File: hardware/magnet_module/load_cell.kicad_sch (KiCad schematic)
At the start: 12 parts, among them J7 691137710004, U4 NAU7802, U5 KC2520Z4.91520C1KX00

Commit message: add titles & esd protection for IO
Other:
- company: (none) -> Christie Lab, CU-Anschultz
- title: (none) -> Autotrainer Magnet Module - Load Cell
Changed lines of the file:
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@@
 	(generator_version "8.0")
 	(paper "A4")
+	(title_block
+		(title "Autotrainer Magnet Module - Load Cell")
+		(date "2024-07-09")
+		(rev "v1.0")
+		(company "Christie Lab, CU-Anschultz")
+		(comment 1 "Prepared by LeafLabs, LLC")
+	)
 	(bus_alias "I2C"
 		(members "SDA" "SCL")

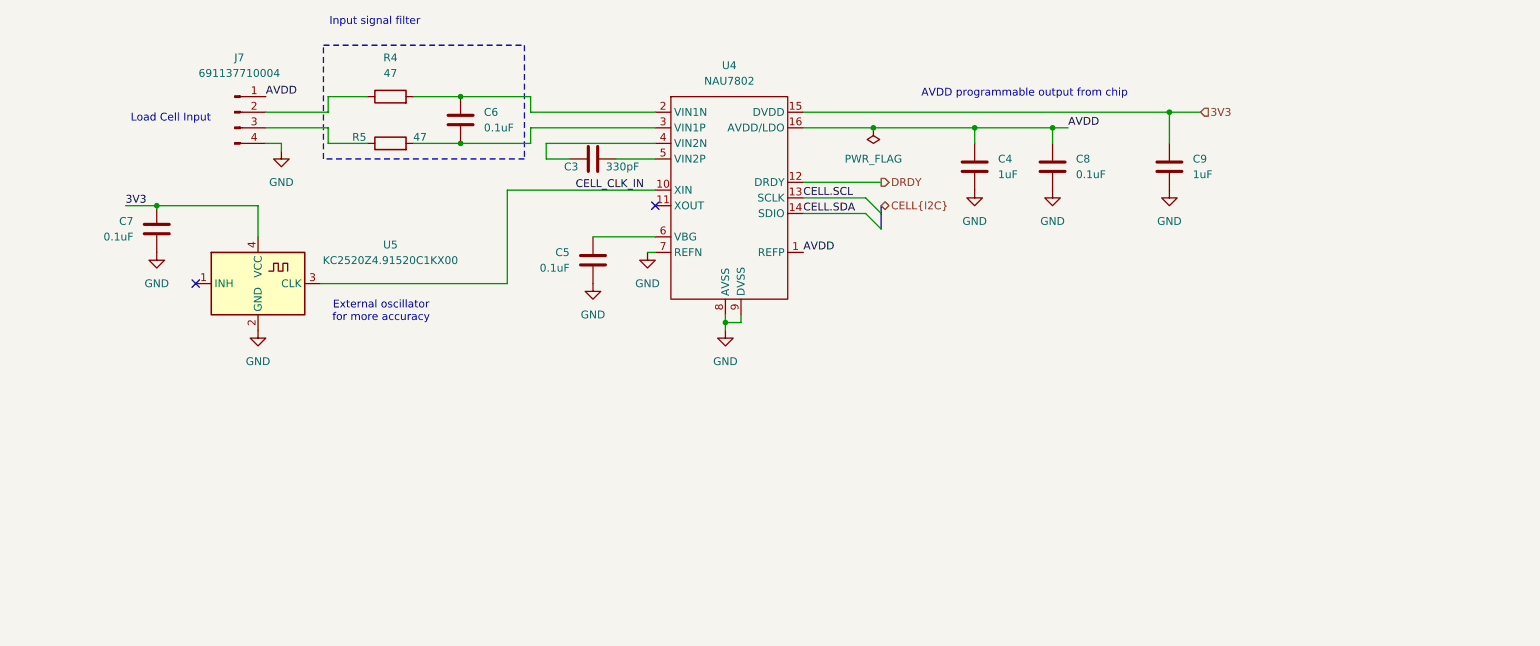
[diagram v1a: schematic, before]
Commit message: add all PNs, relevant datasheets, and test points
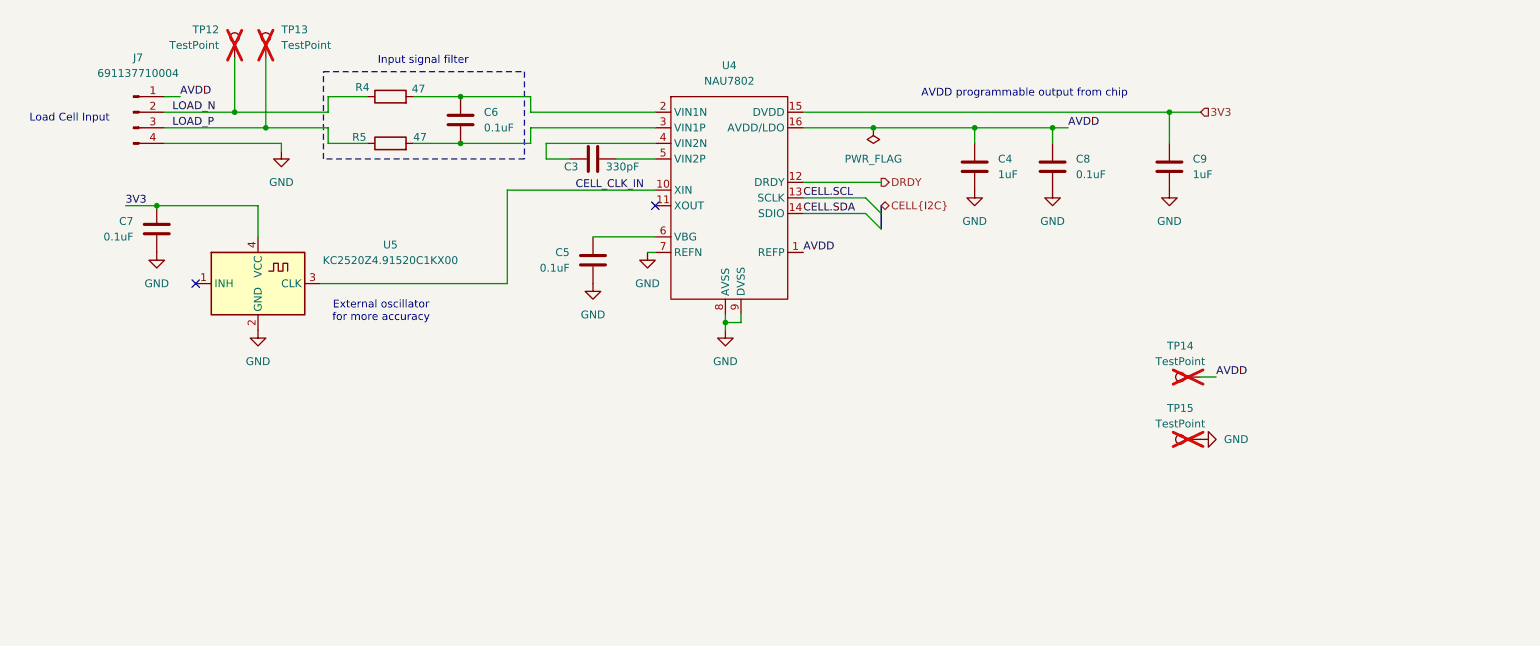
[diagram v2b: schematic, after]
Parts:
- added TP12, TP13, TP14, TP15: TestPoint, symbol Connector:TestPoint
- C3: footprint (none) -> Capacitor_SMD:C_0603_1608Metric; MPN (none) -> C0603C331J5GAC7867
- C4, C5, C6, C7, C8, C9: footprint (none) -> Capacitor_SMD:C_0603_1608Metric; MPN (none) -> CC0603KRX7R7BB104
- J7: MPN (none) -> 691137710004
- R4, R5: MPN (none) -> RC0603FR-0747RL
- U4: MPN (none) -> NAU7802SGI
- U5: MPN (none) -> KC2520Z4.91520C1KX00
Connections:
- net AVDD: now also TP14.1
- net GND: now also TP15.1
- net LOAD_N: now reaches J7.2 (Pin_2), R4.1
- net LOAD_N: now also TP12.1
- net LOAD_P: now reaches J7.3 (Pin_3), R5.1
- net LOAD_P: now also TP13.1
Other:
- moved on the sheet: J7

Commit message: make changes as requested by Ryan
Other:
- company: Christie Lab, CU-Anschultz -> Christie Lab, CU-Anschutz
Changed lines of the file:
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@@
 		(date "2024-07-09")
 		(rev "v1.0")
-		(company "Christie Lab, CU-Anschultz")
+		(company "Christie Lab, CU-Anschutz")
 		(comment 1 "Prepared by LeafLabs, LLC")
 	)

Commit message: make changes requested by dan, run ERC
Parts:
- TP12, TP13, TP14, TP15: now fitted; now left out of the parts list
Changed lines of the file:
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@@
 		(unit 1)
 		(exclude_from_sim no)
-		(in_bom yes)
-		(on_board yes)
-		(dnp yes)
+		(in_bom no)
+		(on_board yes)
+		(dnp no)
 		(property "Reference" "TP12"
 			(at 60.96 57.6579 0)
@@
 		(unit 1)
 		(exclude_from_sim no)
-		(in_bom yes)
-		(on_board yes)
-		(dnp yes)
+		(in_bom no)
+		(on_board yes)
+		(dnp no)
 		(fields_autoplaced yes)
 		(property "Reference" "TP15"
@@
 		(unit 1)
 		(exclude_from_sim no)
-		(in_bom yes)
-		(on_board yes)
-		(dnp yes)
+		(in_bom no)
+		(on_board yes)
+		(dnp no)
 		(fields_autoplaced yes)
 		(property "Reference" "TP14"
@@
 		(unit 1)
 		(exclude_from_sim no)
-		(in_bom yes)
-		(on_board yes)
-		(dnp yes)
+		(in_bom no)
+		(on_board yes)
+		(dnp no)
 		(fields_autoplaced yes)
 		(property "Reference" "TP13"

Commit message: add footprints & 3d models for magnet module connector placmeent
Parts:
- J7: footprint (none) -> TerminalBlock_RND:TerminalBlock_RND_205-00003_1x04_P5.00mm_Horizontal
- R4, R5: footprint (none) -> Resistor_SMD:R_0603_1608Metric
- TP12, TP13, TP14, TP15: footprint (none) -> TestPoint:TestPoint_Pad_1.0x1.0mm
- U4: footprint (none) -> Package_SO:SOP-16_3.9x9.9mm_P1.27mm
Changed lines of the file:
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@@
 			)
 		)
-		(property "Footprint" ""
+		(property "Footprint" "Resistor_SMD:R_0603_1608Metric"
 			(at 88.9 70.358 90)
 			(effects
@@
 			)
 		)
-		(property "Footprint" ""
+		(property "Footprint" "TestPoint:TestPoint_Pad_1.0x1.0mm"
 			(at 58.42 62.23 0)
 			(effects
@@
 			)
 		)
-		(property "Footprint" ""
+		(property "Footprint" "TestPoint:TestPoint_Pad_1.0x1.0mm"
 			(at 220.98 119.38 0)
 			(effects
@@
 			)
 		)
-		(property "Footprint" ""
+		(property "Footprint" "TestPoint:TestPoint_Pad_1.0x1.0mm"
 			(at 220.98 109.22 0)
 			(effects
@@
 			)
 		)
-		(property "Footprint" ""
+		(property "Footprint" "TestPoint:TestPoint_Pad_1.0x1.0mm"
 			(at 73.66 62.23 0)
 			(effects
@@
 			)
 		)
-		(property "Footprint" ""
+		(property "Footprint" "TerminalBlock_RND:TerminalBlock_RND_205-00003_1x04_P5.00mm_Horizontal"
 			(at 46.99 71.12 0)
 			(effects
@@
 			)
 		)
-		(property "Footprint" ""
+		(property "Footprint" "Package_SO:SOP-16_3.9x9.9mm_P1.27mm"
 			(at 144.78 64.77 0)
 			(effects
@@
 			)
 		)
-		(property "Footprint" ""
+		(property "Footprint" "Resistor_SMD:R_0603_1608Metric"
 			(at 88.9 77.978 90)
 			(effects

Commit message: Releases layout for pellet, magnet, and Jetson breakout boards.
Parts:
- added R21, R22: 4.7k, Resistor_SMD:R_0603_1608Metric, symbol Device:R
- C3: LCSC (none) -> C1664; MPN C0603C331J5GAC7867 -> CL10C331JB8NNNC
- C4, C9: LCSC (none) -> C15849; MPN CC0603KRX7R7BB104 -> CL10A105KB8NNNC
- C5, C6, C7, C8: LCSC (none) -> C14663; MPN CC0603KRX7R7BB104 -> CC0603KRX7R9BB104
- J7: LCSC (none) -> C7032066
- R4, R5: LCSC (none) -> C23182; MPN RC0603FR-0747RL -> 0603WAF470JT5E
- U4: LCSC (none) -> C5180029
- U5: LCSC (none) -> C17562469
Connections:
- net 3V3: now also R21.1, R22.1
- net CELL.SCL: now also R21.2
- net CELL.SDA: now also R22.2
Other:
- note added: "I2C Pullups"
